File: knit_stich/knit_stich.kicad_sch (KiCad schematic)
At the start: 0 parts

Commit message: added 2x3 connector
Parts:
- added J1: Conn_02x03_Counter_Clockwise, Connector_PinHeader_2.54mm:PinHeader_2x03_P2.54mm_Vertical, symbol Connector_Generic:Conn_02x03_Counter_Clockwise
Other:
- company: (none) -> Boris Nimcevic
- title: (none) -> knit stitch pattern
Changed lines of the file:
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@@
 	(generator_version "9.0")
 	(paper "A4")
+	(title_block
+		(title "knit stitch pattern")
+		(date "2025-07-26")
+		(rev "v1")
+		(company "Boris Nimcevic")
+	)
+	(symbol
+		(lib_id "Connector_Generic:Conn_02x03_Counter_Clockwise")
+		(at 157.48 68.58 0)
+		(unit 1)
+		(exclude_from_sim no)
+		(in_bom yes)
+		(on_board yes)
+		(dnp no)
+		(fields_autoplaced yes)
+		(property "Reference" "J1"
+			(at 158.75 59.69 0)
+			(effects
+				(font
+					(size 1.27 1.27)
+				)
+			)
+		)
+		(property "Value" "Conn_02x03_Counter_Clockwise"
+			(at 158.75 62.23 0)
+			(effects
+				(font
+					(size 1.27 1.27)
+				)
+			)
+		)
+		(property "Footprint" "Connector_PinHeader_2.54mm:PinHeader_2x03_P2.54mm_Vertical"
+			(at 157.48 68.58 0)
+			(effects
+				(font
+					(size 1.27 1.27)
+				)
+				(hide yes)
+			)
+		)
+		(property "Datasheet" "~"
+			(at 157.48 68.58 0)
+			(effects
+				(font
+					(size 1.27 1.27)
+				)
+				(hide yes)
+			)
+		)
+		(property "Description" "Generic connector, double row, 02x03, counter clockwise pin numbering scheme (similar to DIP package numbering), script generated (kicad-library-utils/schlib/autogen/connector/)"
+			(at 157.48 68.58 0)
+			(effects
+				(font
+					(size 1.27 1.27)
+				)
+				(hide yes)
+			)
+		)
+		(pin "3"
+		)
+		(pin "6"
+		)
+		(pin "5"
+		)
+		(pin "4"
+		)
+		(pin "2"
+		)
+		(pin "1"
+		)
+		(instances
+			(project ""
+				(path "/04b7b4b8-52af-4126-b4f3-54c99bc27a2f"
+					(reference "J1")
+					(unit 1)
+				)
+			)
+		)
+	)
 	(sheet_instances
 		(path "/"

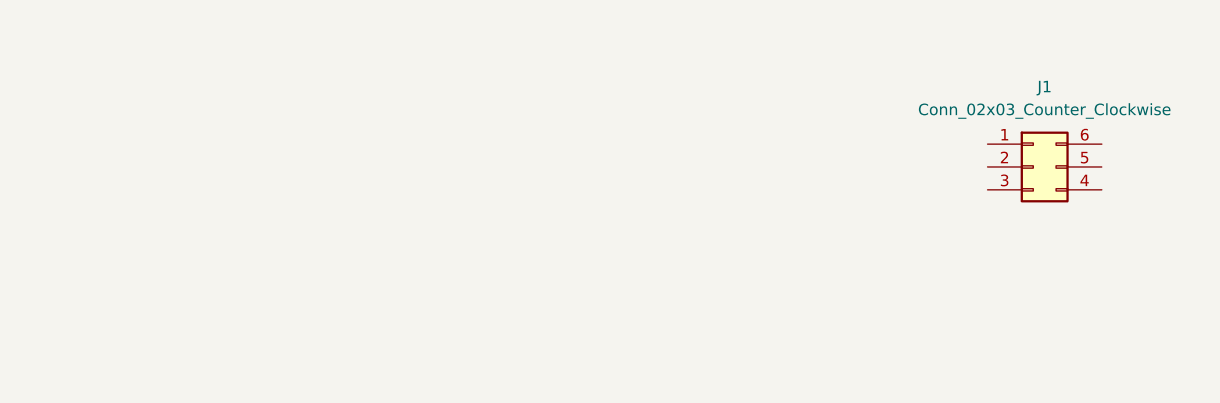
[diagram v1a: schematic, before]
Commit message: added LEDs to the schematic|
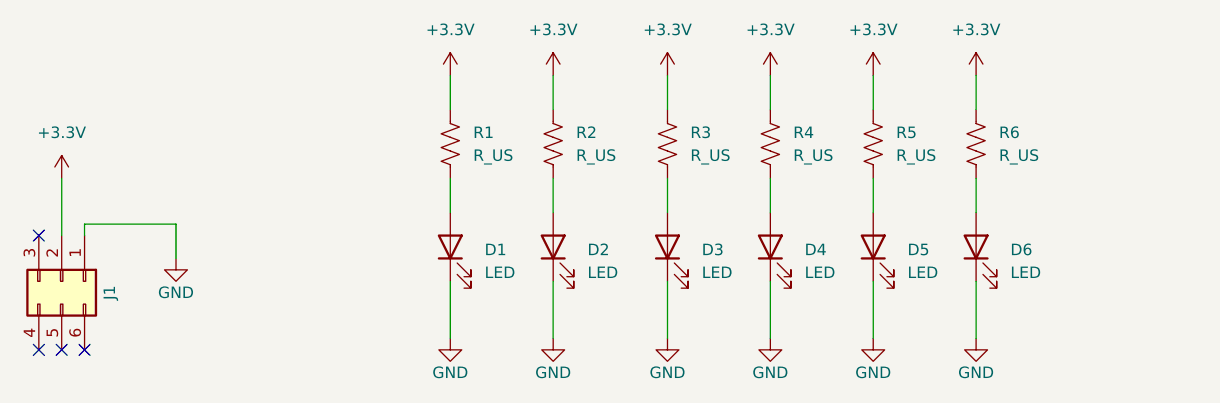
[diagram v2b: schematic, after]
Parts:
- added D1, D2, D3, D4, D5, D6: LED, LED_SMD:LED_0603_1608Metric_Pad1.05x0.95mm_HandSolder, symbol Device:LED
- added R1, R2, R3, R4, R5, R6: R_US, Resistor_SMD:R_0603_1608Metric_Pad0.98x0.95mm_HandSolder, symbol Device:R_US
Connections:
- net GND: now reaches J1.1 (Pin_1)
- net GND: now also D1.1 (K), D2.1 (K), D3.1 (K), D4.1 (K), D5.1 (K), D6.1 (K)
- net +3.3V: now reaches J1.2 (Pin_2)
- net +3.3V: now also R1.1, R2.1, R3.1, R4.1, R5.1, R6.1
- new net: D3.2 (A), R3.2
- new net: D2.2 (A), R2.2
- new net: D6.2 (A), R6.2
- new net: D5.2 (A), R5.2
- new net: D1.2 (A), R1.2
- new net: D4.2 (A), R4.2
- no-connect marks 0 -> 4
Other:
- moved on the sheet: J1
